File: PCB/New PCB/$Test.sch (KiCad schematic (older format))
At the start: 52 parts, among them P10 CONN_2, P11 CONN_2, P12 CONN_1, P13 CONN_1, P14 CONN_1, P15 CONN_1, P16 CONN_6, P17 CONN_1, P18 CONN_1, P19 CONN_2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

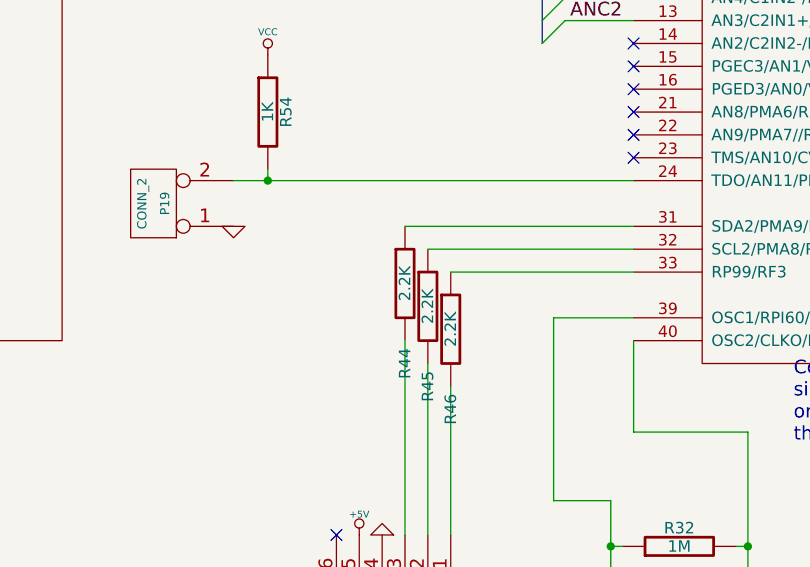
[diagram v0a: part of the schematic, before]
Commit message: Updated Motor/Magnet PCB
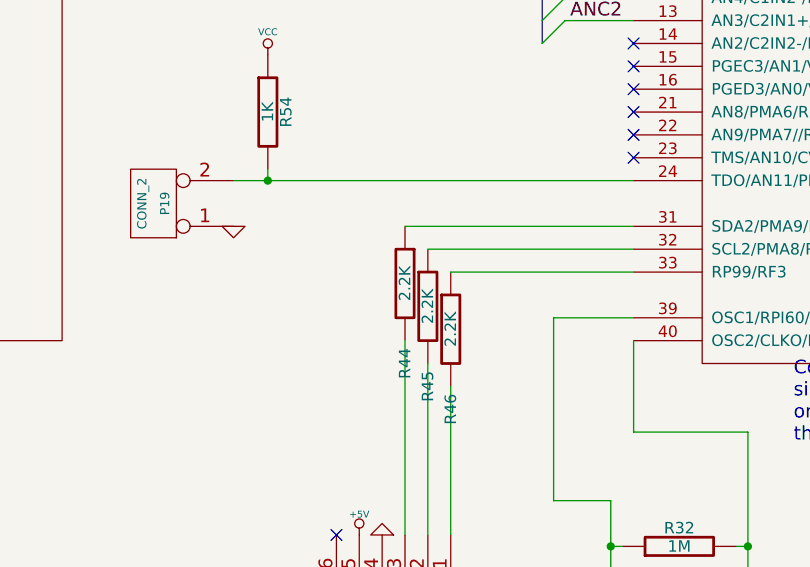
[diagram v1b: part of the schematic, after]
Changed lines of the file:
@@
 Sheet 1 4
 Title ""
-Date "27 jun 2013"
+Date "28 jun 2013"
 Rev ""
 Comp ""
@@
 F 3 "~" H 7100 9000 60  0000 C CNN
 	1    7100 9000
-	1    0    0    -1
-$EndComp
-$Comp
+	-1   0    0    -1
+$EndComp
+$Comp
